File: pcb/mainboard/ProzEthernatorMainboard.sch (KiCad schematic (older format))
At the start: 0 parts

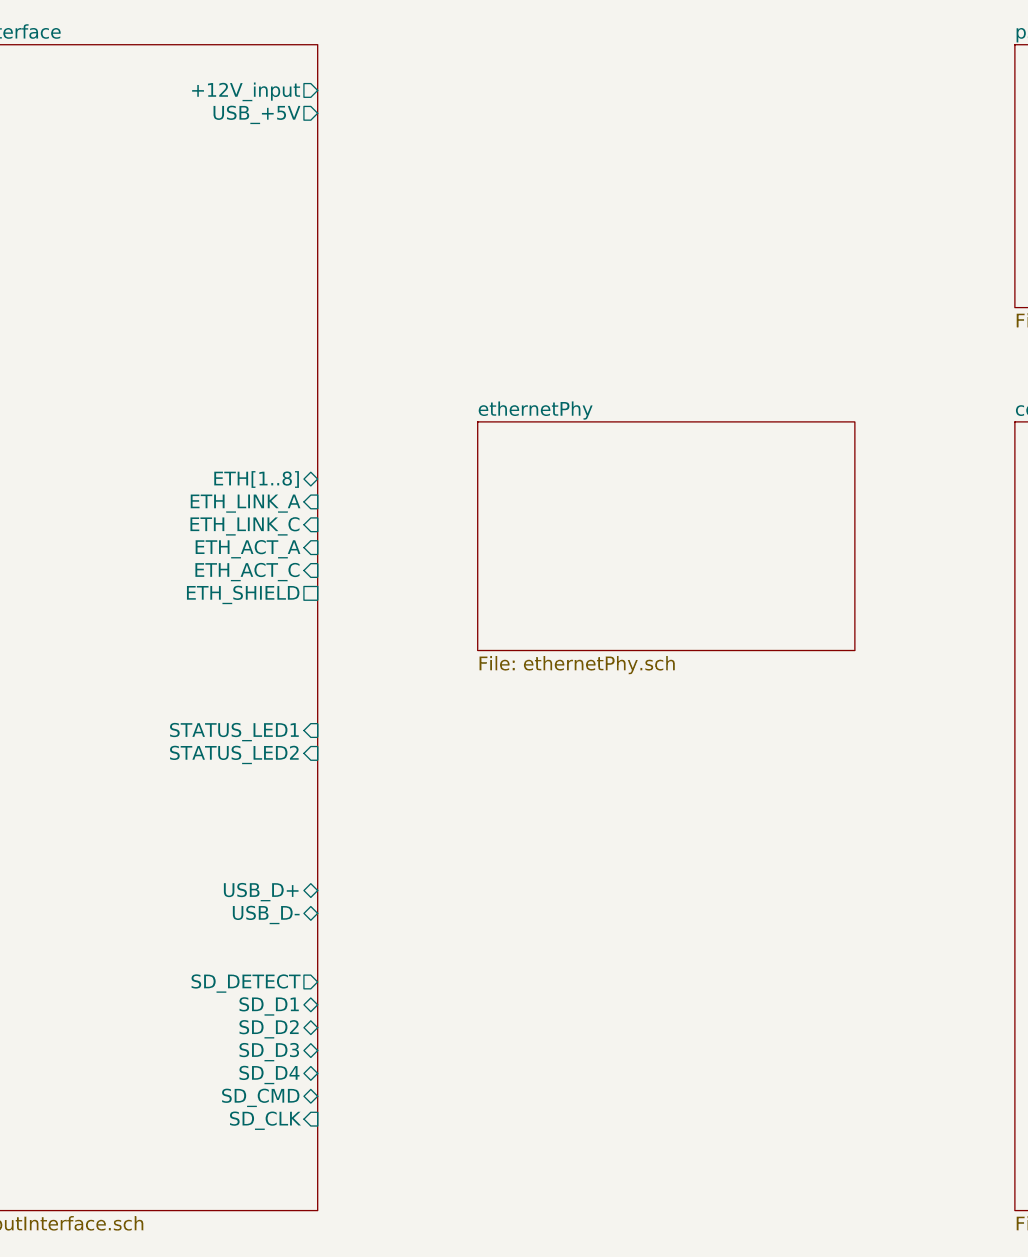
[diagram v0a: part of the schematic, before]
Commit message: worked on PoE regulator
Added the SRAM
Added an EEPROM and a FLASH as nonvolatileMemory
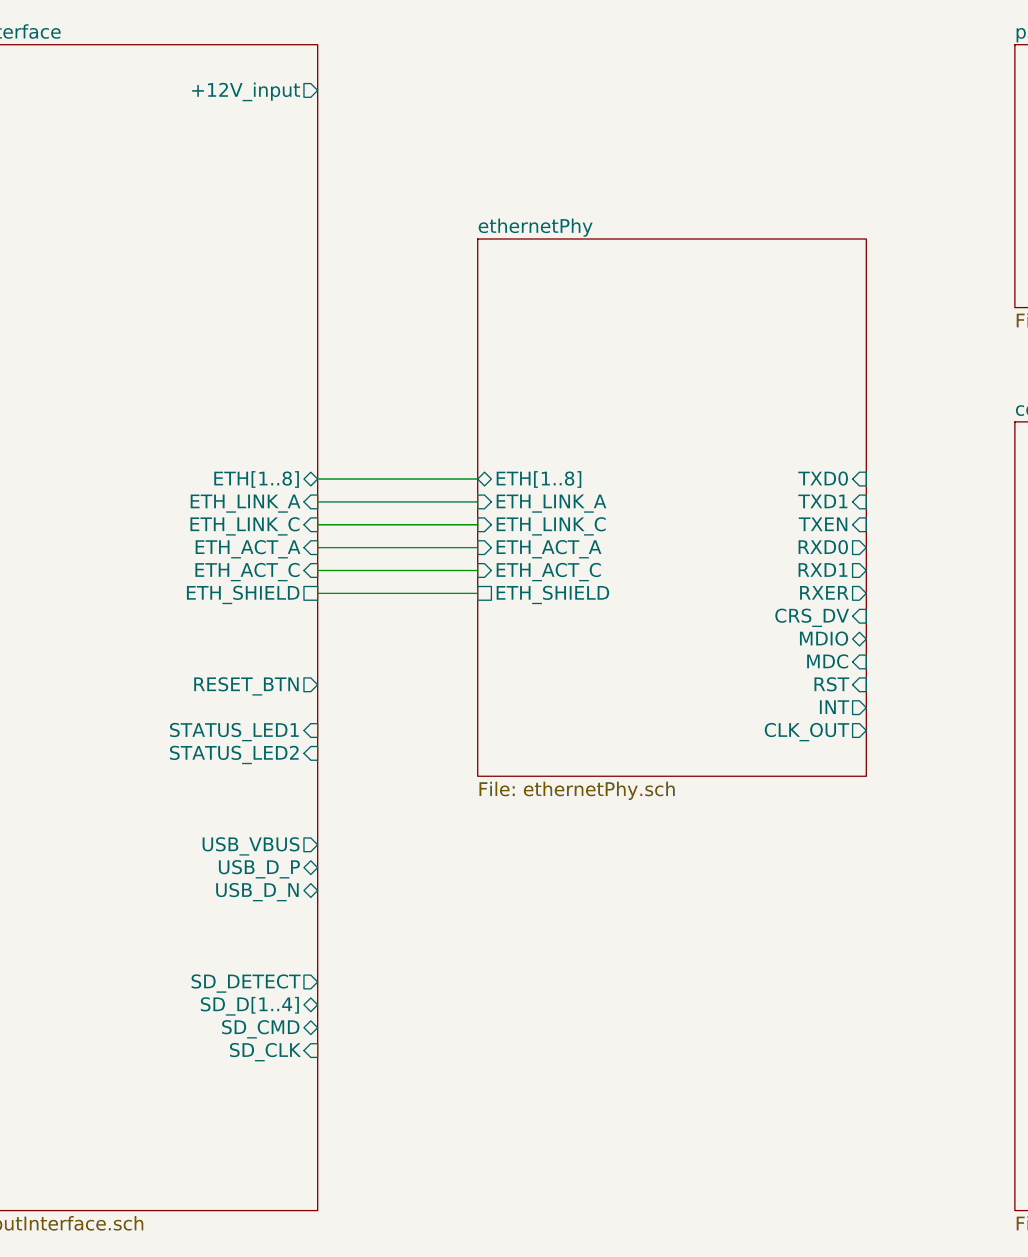
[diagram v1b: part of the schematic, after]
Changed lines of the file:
@@
 $Descr A4 11693 8268
 encoding utf-8
-Sheet 1 9
+Sheet 1 10
 Title "ProzEthernatorMainboard"
 Date "2018-02-08"
@@
 Comment4 ""
 $EndDescr
-$Sheet
-S 800  850  1700 5100
-U 5A7C790D
-F0 "inputInterface" 60
-F1 "inputInterface.sch" 60
-F2 "+12V_input" O R 2500 1050 60
-F3 "USB_+5V" O R 2500 1150 60
-F4 "USB_D+" B R 2500 4550 60
-F5 "USB_D-" B R 2500 4650 60
-F6 "SD_DETECT" O R 2500 4950 60
-F7 "SD_D1" B R 2500 5050 60
-F8 "SD_D2" B R 2500 5150 60
-F9 "SD_D3" B R 2500 5250 60
-F10 "SD_D4" B R 2500 5350 60
-F11 "SD_CMD" B R 2500 5450 60
-F12 "SD_CLK" I R 2500 5550 60
-F13 "ETH[1..8]" B R 2500 2750 60
-F14 "ETH_LINK_A" I R 2500 2850 60
-F15 "ETH_LINK_C" I R 2500 2950 60
-F16 "ETH_ACT_A" I R 2500 3050 60
-F17 "ETH_ACT_C" I R 2500 3150 60
-F18 "ETH_SHIELD" U R 2500 3250 60
-F19 "STATUS_LED1" I R 2500 3850 60
-F20 "STATUS_LED2" I R 2500 3950 60
-$EndSheet
 $Sheet
 S 5550 2500 1650 3450
@@
 $EndSheet
 $Sheet
-S 3200 2500 1650 1000
+S 3200 1700 1700 2350
 U 5A7C7923
 F0 "ethernetPhy" 60
 F1 "ethernetPhy.sch" 60
+F2 "ETH[1..8]" B L 3200 2750 60
+F3 "ETH_LINK_A" I L 3200 2850 60
+F4 "ETH_LINK_C" I L 3200 2950 60
+F5 "ETH_ACT_A" I L 3200 3050 60
+F6 "ETH_ACT_C" I L 3200 3150 60
+F7 "ETH_SHIELD" U L 3200 3250 60
+F8 "TXD0" I R 4900 2750 60
+F9 "TXD1" I R 4900 2850 60
+F10 "TXEN" I R 4900 2950 60
+F11 "RXD0" O R 4900 3050 60
+F12 "RXD1" O R 4900 3150 60
+F13 "RXER" O R 4900 3250 60
+F14 "CRS_DV" I R 4900 3350 60
+F15 "MDIO" B R 4900 3450 60
+F16 "MDC" I R 4900 3550 60
+F17 "RST" I R 4900 3650 60
+F18 "INT" O R 4900 3750 60
+F19 "CLK_OUT" O R 4900 3850 60
 $EndSheet
+$Sheet
+S 800  850  1700 5100
+U 5A7C790D
+F0 "inputInterface" 60
+F1 "inputInterface.sch" 60
+F2 "+12V_input" O R 2500 1050 60
+F3 "SD_DETECT" O R 2500 4950 60
+F4 "SD_CMD" B R 2500 5150 60
+F5 "SD_CLK" I R 2500 5250 60
+F6 "ETH[1..8]" B R 2500 2750 60
+F7 "ETH_LINK_A" I R 2500 2850 60
+F8 "ETH_LINK_C" I R 2500 2950 60
+F9 "ETH_ACT_A" I R 2500 3050 60
+F10 "ETH_ACT_C" I R 2500 3150 60
+F11 "ETH_SHIELD" U R 2500 3250 60
+F12 "STATUS_LED1" I R 2500 3850 60
+F13 "STATUS_LED2" I R 2500 3950 60
+F14 "SD_D[1..4]" B R 2500 5050 60
+F15 "USB_VBUS" O R 2500 4350 60
+F16 "USB_D_P" B R 2500 4450 60
+F17 "USB_D_N" B R 2500 4550 60
+F18 "RESET_BTN" O R 2500 3650 60
+$EndSheet
+Wire Wire Line
+	2500 2750 3200 2750
+Wire Wire Line
+	2500 2850 3200 2850
+Wire Wire Line
+	2500 2950 3200 2950
+Wire Wire Line
+	2500 3050 3200 3050
+Wire Wire Line
+	2500 3150 3200 3150
+Wire Wire Line
+	2500 3250 3200 3250
 $EndSCHEMATC
